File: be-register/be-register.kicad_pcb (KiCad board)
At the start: 2 copper layers, 24 parts, among them J1 Conn_01x02, J2 Conn_01x08, J3 Conn_01x04, J4 Conn_01x08, U1 74LS173, U2 74LS173, U3 74LS245, U4 ULN2803A

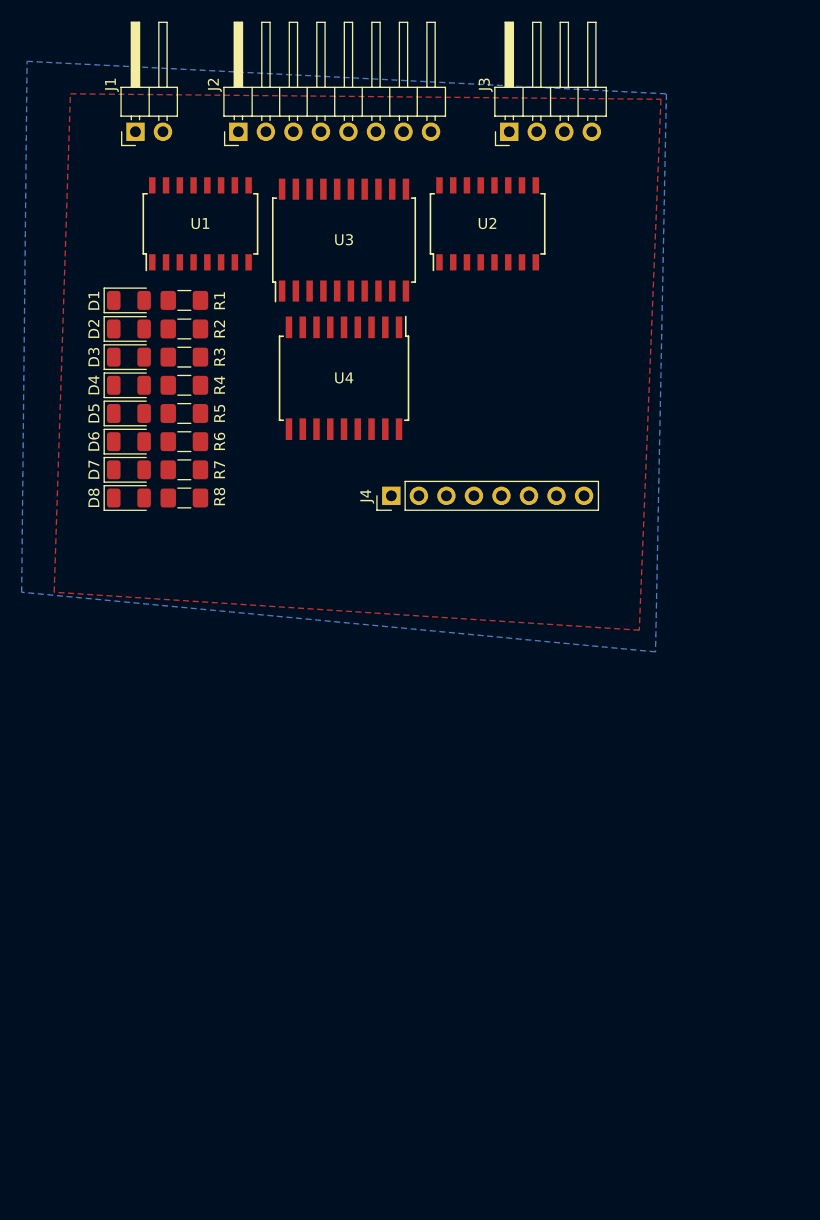
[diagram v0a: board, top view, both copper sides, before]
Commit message: laying out and wiring up the register module
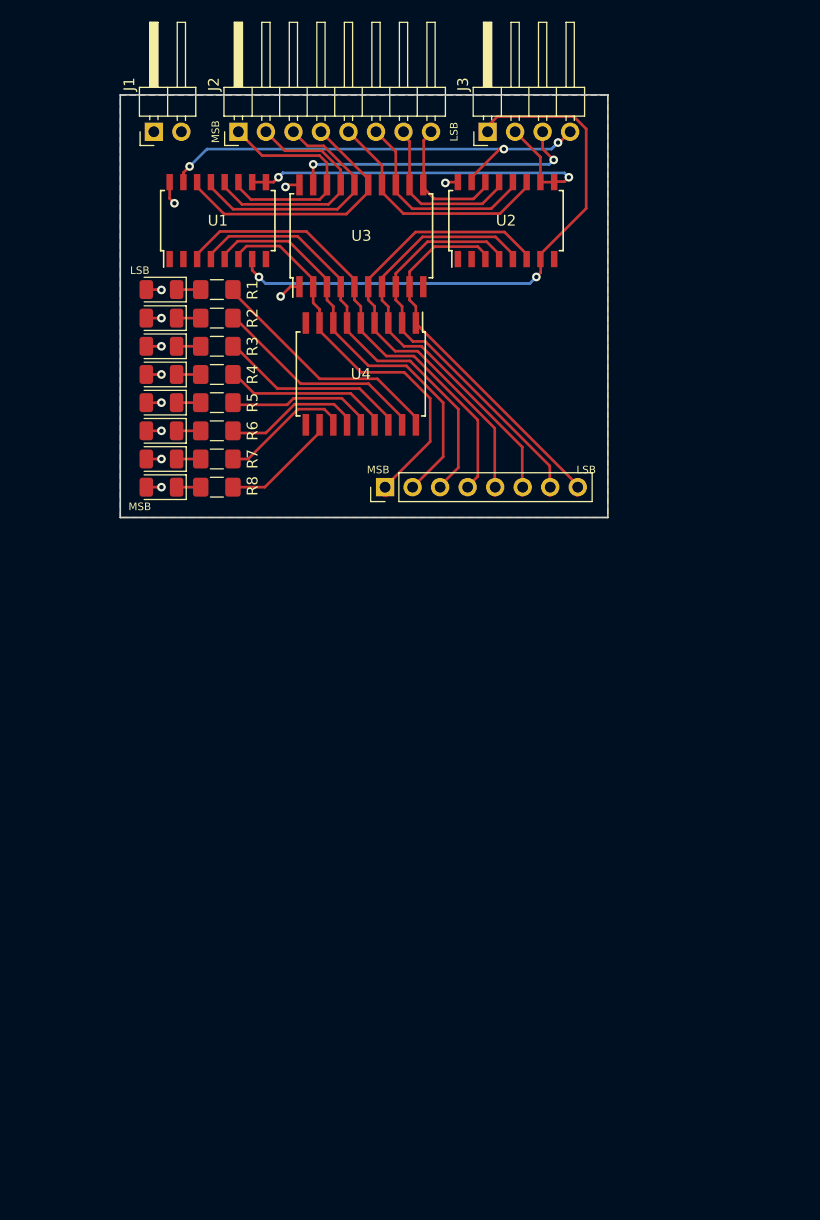
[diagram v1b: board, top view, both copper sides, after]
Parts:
- moved D1 3.16 mm to (136.4, 65.6), turned to 180 degrees
- moved D2 3.16 mm to (136.4, 68.2), turned to 180 degrees
- moved D3 3.16 mm to (136.4, 70.8), turned to 180 degrees
- moved D4 3.16 mm to (136.4, 73.4), turned to 180 degrees
- moved D5 3.16 mm to (136.4, 76.0), turned to 180 degrees
- moved D6 3.16 mm to (136.4, 78.6), turned to 180 degrees
- moved D7 3.16 mm to (136.4, 81.2), turned to 180 degrees
- moved D8 3.16 mm to (136.4, 83.8), turned to 180 degrees
- moved R1 3.16 mm to (141.5, 65.6)
- moved R2 3.16 mm to (141.5, 68.2)
- moved R3 3.16 mm to (141.5, 70.8)
- moved R4 3.16 mm to (141.5, 73.4)
- moved R5 3.16 mm to (141.5, 76.0)
- moved R6 3.16 mm to (141.5, 78.6)
- moved R7 3.16 mm to (141.5, 81.2)
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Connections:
- D1 pad 1: GND -> Net-(D1-Pad1)
- D1 pad 2: Net-(D1-Pad2) -> VCC
- D2 pad 1: GND -> Net-(D2-Pad1)
- D2 pad 2: Net-(D2-Pad2) -> VCC
- D3 pad 1: GND -> Net-(D3-Pad1)
- D3 pad 2: Net-(D3-Pad2) -> VCC
- D4 pad 1: GND -> Net-(D4-Pad1)
- D4 pad 2: Net-(D4-Pad2) -> VCC
- D5 pad 1: GND -> Net-(D5-Pad1)
- D5 pad 2: Net-(D5-Pad2) -> VCC
- D6 pad 1: GND -> Net-(D6-Pad1)
- D6 pad 2: Net-(D6-Pad2) -> VCC
- D7 pad 1: GND -> Net-(D7-Pad1)
- D7 pad 2: Net-(D7-Pad2) -> VCC
- D8 pad 1: GND -> Net-(D8-Pad1)
- D8 pad 2: Net-(D8-Pad2) -> VCC
- R1 pad 1: Net-(D1-Pad2) -> Net-(D1-Pad1)
- R2 pad 1: Net-(D2-Pad2) -> Net-(D2-Pad1)
- R3 pad 1: Net-(D3-Pad2) -> Net-(D3-Pad1)
- R4 pad 1: Net-(D4-Pad2) -> Net-(D4-Pad1)
- R5 pad 1: Net-(D5-Pad2) -> Net-(D5-Pad1)
- R6 pad 1: Net-(D6-Pad2) -> Net-(D6-Pad1)
- R7 pad 1: Net-(D7-Pad2) -> Net-(D7-Pad1)
- R8 pad 1: Net-(D8-Pad2) -> Net-(D8-Pad1)
- U1 pad 11: /BUS3 -> /BUS0
- U1 pad 12: /BUS2 -> /BUS1
- U1 pad 13: /BUS1 -> /BUS2
- U1 pad 14: /BUS0 -> /BUS3
- U1 pad 3: /RAW0 -> /RAW3
- U1 pad 4: /RAW1 -> /RAW2
- U1 pad 5: /RAW2 -> /RAW1
- U1 pad 6: /RAW3 -> /RAW0
- U2 pad 11: /BUS7 -> /BUS4
- U2 pad 12: /BUS6 -> /BUS5
- U2 pad 13: /BUS5 -> /BUS6
- U2 pad 14: /BUS4 -> /BUS7
- U2 pad 3: /RAW4 -> /RAW7
- U2 pad 4: /RAW5 -> /RAW6
- U2 pad 5: /RAW6 -> /RAW5
- U2 pad 6: /RAW7 -> /RAW4
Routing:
- net /CLK: track 0.00 -> 54.0 mm, vias 0 -> 2
- net /RAW4: track 0.00 -> 43.8 mm
- net /RAW3: track 0.00 -> 43.5 mm
- net /RST: track 0.00 -> 42.6 mm, vias 0 -> 3
- net /RAW5: track 0.00 -> 41.2 mm
- net /RAW2: track 0.00 -> 40.9 mm
- net /RAW6: track 0.00 -> 38.8 mm
- net /RAW1: track 0.00 -> 38.7 mm
- net /~IE: track 0.00 -> 38.2 mm, vias 0 -> 2
- net /RAW0: track 0.00 -> 36.8 mm
- net /RAW7: track 0.00 -> 35.8 mm
- net /~OE: track 0.00 -> 27.3 mm, vias 0 -> 2
- net /BUS3: track 0.00 -> 25.6 mm
- net /BUS2: track 0.00 -> 24.0 mm
- net /BUS1: track 0.00 -> 22.7 mm
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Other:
- board outline added: 45 x 39 mm
- board text added: "LSB"
- board text added: "MSB"

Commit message: labeling pins and rotating 180, to make all ICs look correct
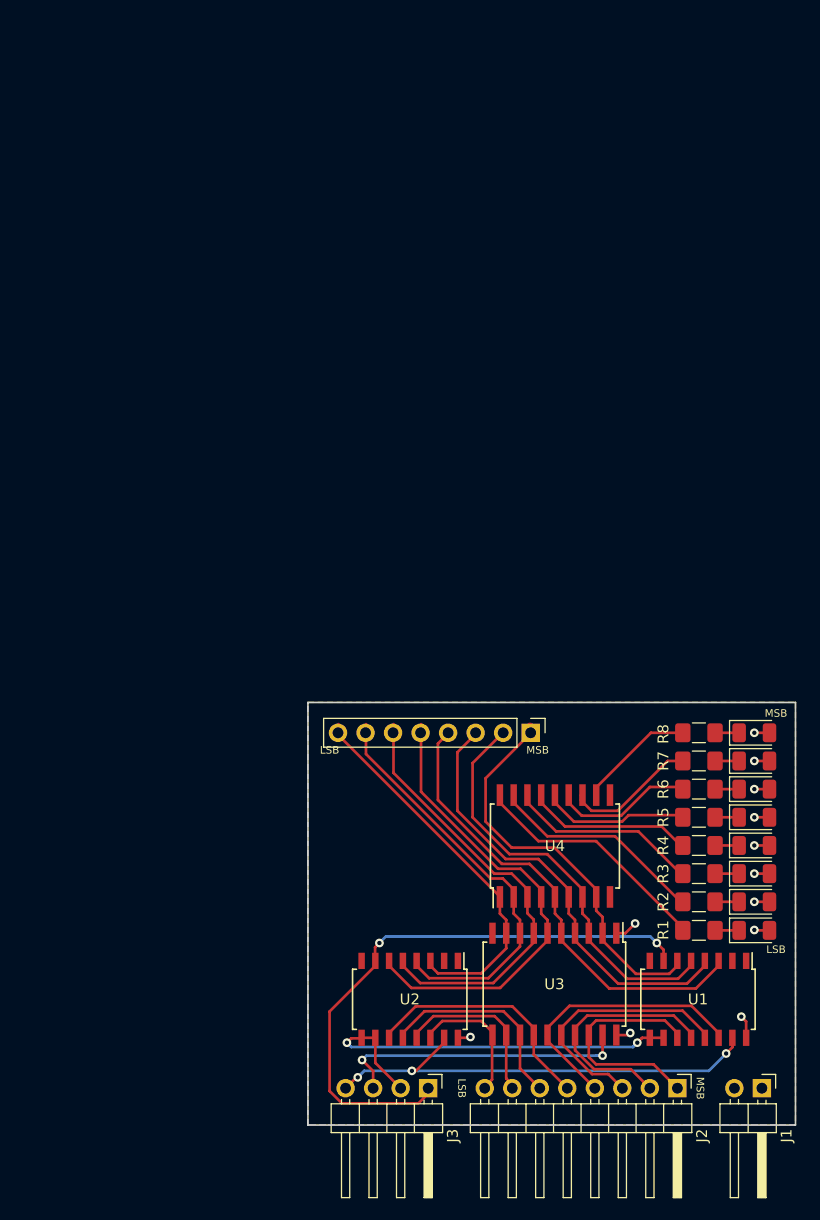
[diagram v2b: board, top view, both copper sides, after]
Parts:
- moved J1 104.6 mm to (191.8, 139.3), turned to 270 degrees
- moved J2 97.1 mm to (184.0, 139.3), turned to 270 degrees
- moved J3 88.4 mm to (161.0, 139.3), turned to 270 degrees
- moved U1 84.4 mm to (185.9, 131.1), turned to 270 degrees
- moved D1 80.6 mm to (191.1, 124.7), turned to 0 degrees
- moved D2 76.8 mm to (191.1, 122.1), turned to 0 degrees
- moved R1 74.0 mm to (186.0, 124.7), turned to 180 degrees
- moved D3 73.2 mm to (191.1, 119.5), turned to 0 degrees
- moved U2 72.4 mm to (159.3, 131.1), turned to 270 degrees
- moved U3 71.3 mm to (172.7, 129.7), turned to 270 degrees
- moved D4 69.9 mm to (191.1, 116.9), turned to 0 degrees
- moved R2 69.9 mm to (186.0, 122.1), turned to 180 degrees
- moved D5 66.8 mm to (191.1, 114.3), turned to 0 degrees
- moved R3 65.9 mm to (186.0, 119.5), turned to 180 degrees
- moved D6 63.9 mm to (191.1, 111.7), turned to 0 degrees
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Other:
- board text added: "BE-REGISTER v0.1"
- board text added: "BUS"
- board text added: "CLK ~IE ~OE RST"
- board text added: "VCC GND"

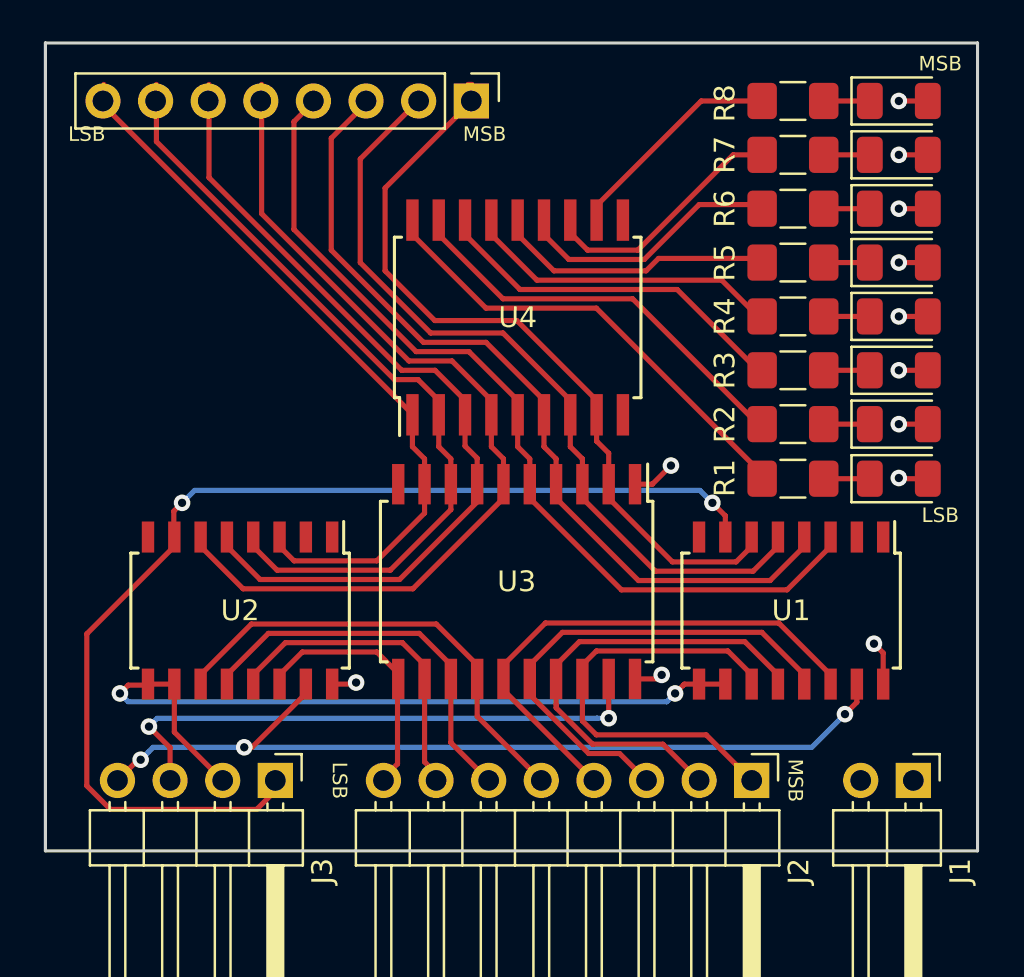
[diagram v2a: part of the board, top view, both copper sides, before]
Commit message: first version of the be-register module
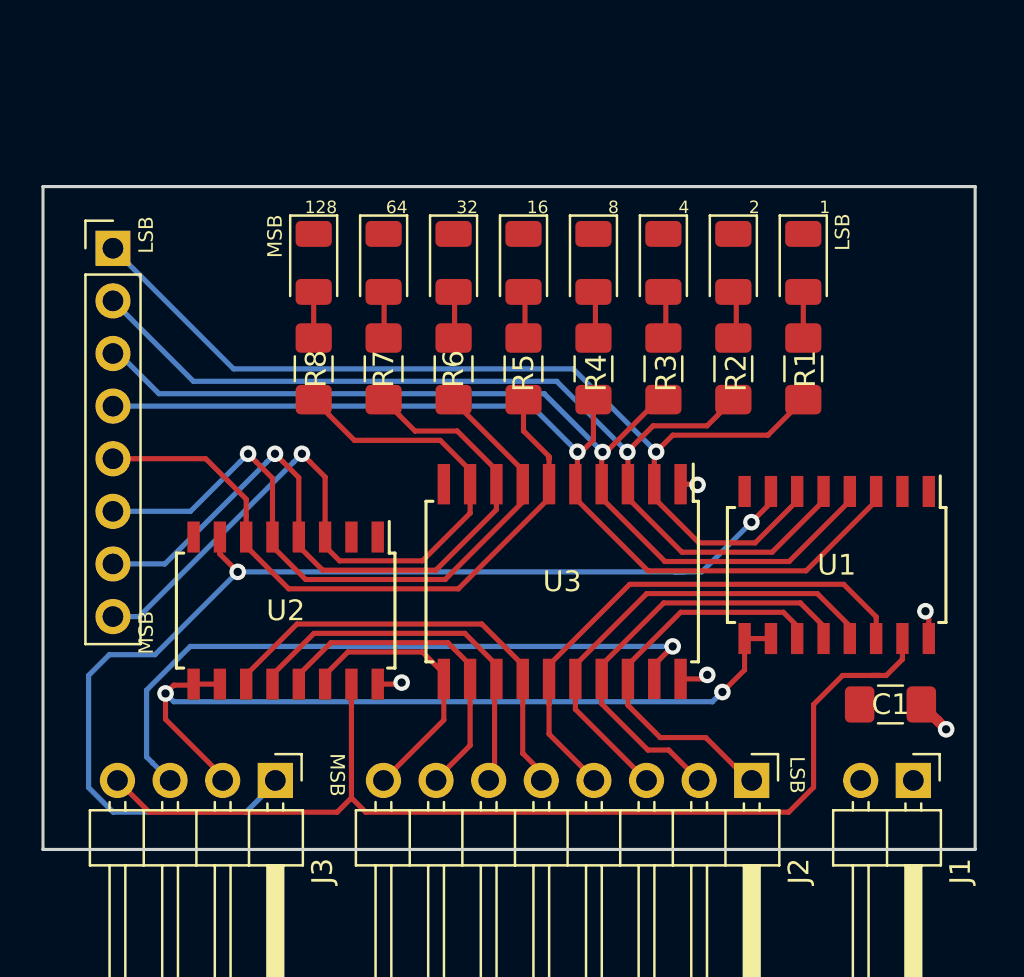
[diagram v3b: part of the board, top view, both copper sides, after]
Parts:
- removed U4: ULN2803A, Package_SO:SOIC-18W_7.5x11.6mm_P1.27mm
- added C1: 0.01u, Capacitor_SMD:C_1206_3216Metric_Pad1.42x1.75mm_HandSolder, F.Cu at (190.7, 135.6)
- moved D8 29.3 mm to (162.9, 114.3), turned to 270 degrees
- moved R8 26.5 mm to (162.9, 119.4), turned to 270 degrees
- moved D7 25.4 mm to (166.2, 114.3), turned to 270 degrees
- moved R7 22.3 mm to (166.2, 119.4), turned to 270 degrees
- moved D6 21.7 mm to (169.6, 114.3), turned to 270 degrees
- moved J4 18.7 mm to (153.2, 113.6), turned to 0 degrees
- moved D5 18.1 mm to (173.0, 114.3), turned to 270 degrees
- moved R6 18.1 mm to (169.6, 119.4), turned to 270 degrees
- moved D4 15.0 mm to (176.4, 114.3), turned to 270 degrees
- moved R5 14.0 mm to (173.0, 119.4), turned to 270 degrees
- moved D3 12.5 mm to (179.7, 114.3), turned to 270 degrees
- moved D1 11.4 mm to (186.5, 114.3), turned to 270 degrees
- moved D2 11.2 mm to (183.1, 114.3), turned to 270 degrees
- moved R4 9.96 mm to (176.4, 119.4), turned to 270 degrees
- moved R3 6.25 mm to (179.7, 119.4), turned to 270 degrees
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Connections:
- D1 pad 1: Net-(D1-Pad1) -> GND
- D1 pad 2: VCC -> Net-(D1-Pad2)
- D2 pad 1: Net-(D2-Pad1) -> GND
- D2 pad 2: VCC -> Net-(D2-Pad2)
- D3 pad 1: Net-(D3-Pad1) -> GND
- D3 pad 2: VCC -> Net-(D3-Pad2)
- D4 pad 1: Net-(D4-Pad1) -> GND
- D4 pad 2: VCC -> Net-(D4-Pad2)
- D5 pad 1: Net-(D5-Pad1) -> GND
- D5 pad 2: VCC -> Net-(D5-Pad2)
- D6 pad 1: Net-(D6-Pad1) -> GND
- D6 pad 2: VCC -> Net-(D6-Pad2)
- D7 pad 1: Net-(D7-Pad1) -> GND
- D7 pad 2: VCC -> Net-(D7-Pad2)
- D8 pad 1: Net-(D8-Pad1) -> GND
- D8 pad 2: VCC -> Net-(D8-Pad2)
- R1 pad 1: Net-(D1-Pad1) -> Net-(D1-Pad2)
- R1 pad 2: Net-(R1-Pad2) -> /RAW0
- R2 pad 1: Net-(D2-Pad1) -> Net-(D2-Pad2)
- R2 pad 2: Net-(R2-Pad2) -> /RAW1
- R3 pad 1: Net-(D3-Pad1) -> Net-(D3-Pad2)
- R3 pad 2: Net-(R3-Pad2) -> /RAW2
- R4 pad 1: Net-(D4-Pad1) -> Net-(D4-Pad2)
- R4 pad 2: Net-(R4-Pad2) -> /RAW3
- R5 pad 1: Net-(D5-Pad1) -> Net-(D5-Pad2)
- R5 pad 2: Net-(R5-Pad2) -> /RAW4
- R6 pad 1: Net-(D6-Pad1) -> Net-(D6-Pad2)
- R6 pad 2: Net-(R6-Pad2) -> /RAW5
- R7 pad 1: Net-(D7-Pad1) -> Net-(D7-Pad2)
- R7 pad 2: Net-(R7-Pad2) -> /RAW6
- R8 pad 1: Net-(D8-Pad1) -> Net-(D8-Pad2)
- R8 pad 2: Net-(R8-Pad2) -> /RAW7
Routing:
- net Net-(R1-Pad2): track 22.0 -> 0.00 mm
- net Net-(R2-Pad2): track 19.3 -> 0.00 mm
- net Net-(R3-Pad2): track 18.0 -> 0.00 mm
- net Net-(R4-Pad2): track 15.8 -> 0.00 mm
- net /RAW0: track 36.8 -> 49.8 mm, vias 0 -> 1
- net Net-(R5-Pad2): track 12.9 -> 0.00 mm
- net Net-(R6-Pad2): track 12.8 -> 0.00 mm
- net Net-(R7-Pad2): track 12.4 -> 0.00 mm
- net /RAW4: track 43.8 -> 32.1 mm
- net VCC: track 18.0 -> 6.47 mm, vias 12 -> 5
- net Net-(R8-Pad2): track 10.9 -> 0.00 mm
- net /RAW1: track 38.7 -> 48.2 mm, vias 0 -> 1
- net /RST: track 42.6 -> 51.4 mm, vias 3 -> 0
- net /RAW5: track 41.2 -> 33.2 mm, vias 0 -> 1
- net /~OE: track 27.3 -> 33.0 mm, vias 2 -> 1
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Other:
- board size 45 x 39 mm -> 45 x 32 mm
- board text added: "1"
- board text added: "128"
- board text added: "16"
- board text added: "2"
- board text added: "32"
- board text added: "4"
- board text added: "64"
- board text added: "8"
